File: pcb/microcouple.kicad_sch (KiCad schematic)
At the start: 34 parts, among them J1 Conn_ARM_SWD_TagConnect_TC203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, J2 USB_C_Socket, SW1 SW_Push, U1 USBLC6-2P6-MS, U2 RP2040, X1 12MHz 12pF

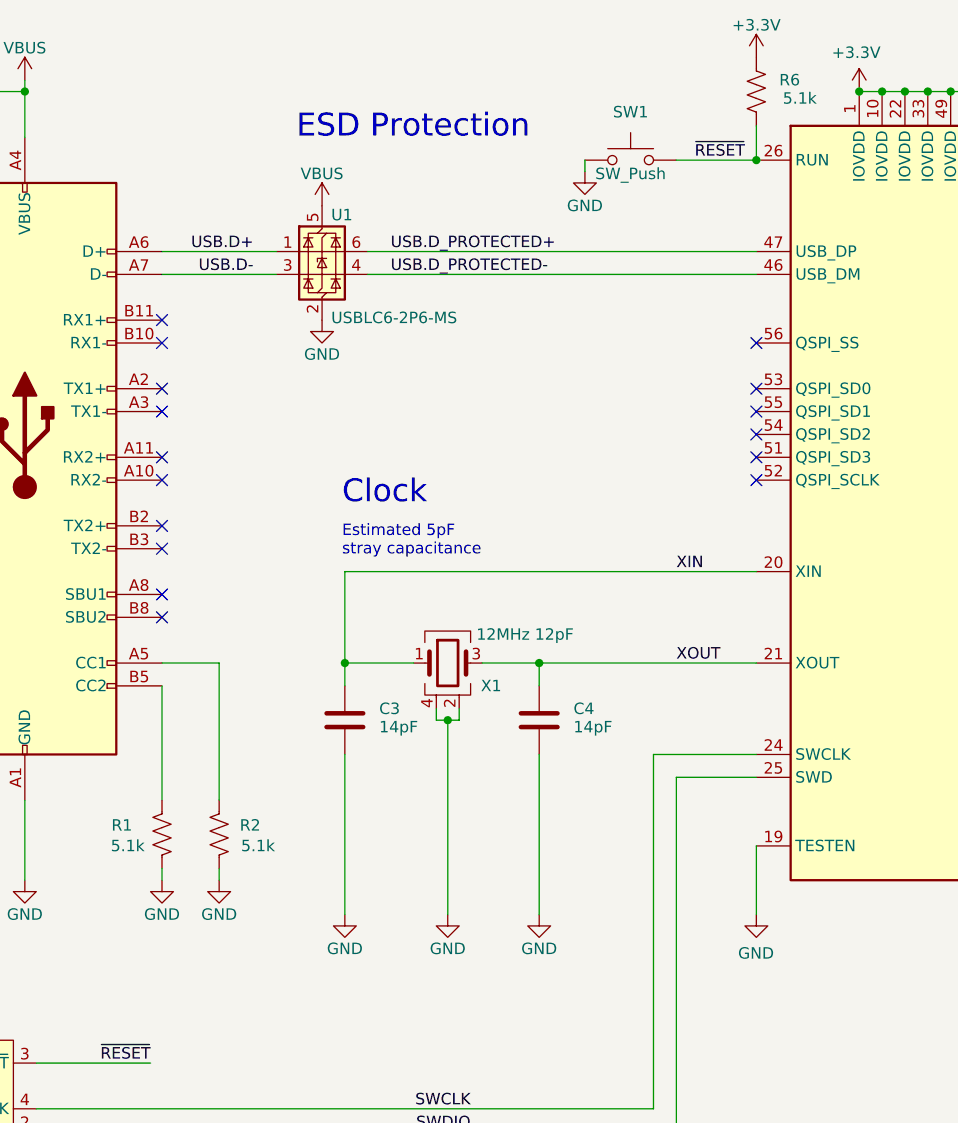
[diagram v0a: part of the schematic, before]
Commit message: Prepare schematic for revision 2.0.0
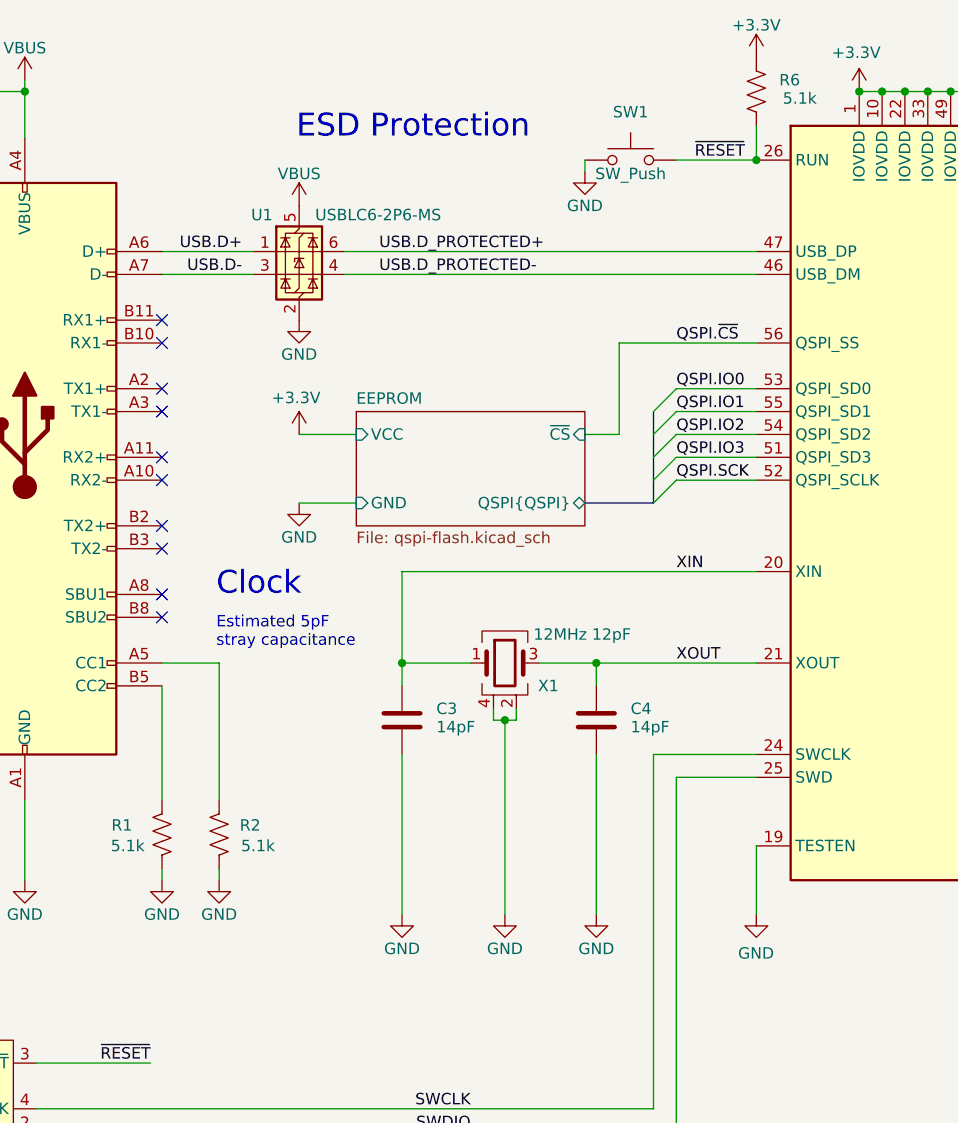
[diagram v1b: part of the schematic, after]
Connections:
- net QSPI.IO3: now reaches U2.51 (QSPI_SD3)
- net QSPI.SCK: now reaches U2.52 (QSPI_SCLK)
- net QSPI.IO0: now reaches U2.53 (QSPI_SD0)
- net QSPI.IO2: now reaches U2.54 (QSPI_SD2)
- net QSPI.IO1: now reaches U2.55 (QSPI_SD1)
- net QSPI.~{CS}: now reaches U2.56 (QSPI_SS)
- no-connect marks 39 -> 33
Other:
- added sheet EEPROM (qspi-flash.kicad_sch)
- moved on the sheet: C3, C4, U1, X1
